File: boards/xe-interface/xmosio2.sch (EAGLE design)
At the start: 105 parts, among them IC1 IDTQS3245QSOP20, IC2 IDTQS3245QSOP20, IC3 IDTQS3245QSOP20, IC4 IDTQS3245QSOP20, IC5 IDTQS3245QSOP20, U1 24 MHz Osc. (F535L-24), U2 USD-SOCKETNEW, X1 0446200002

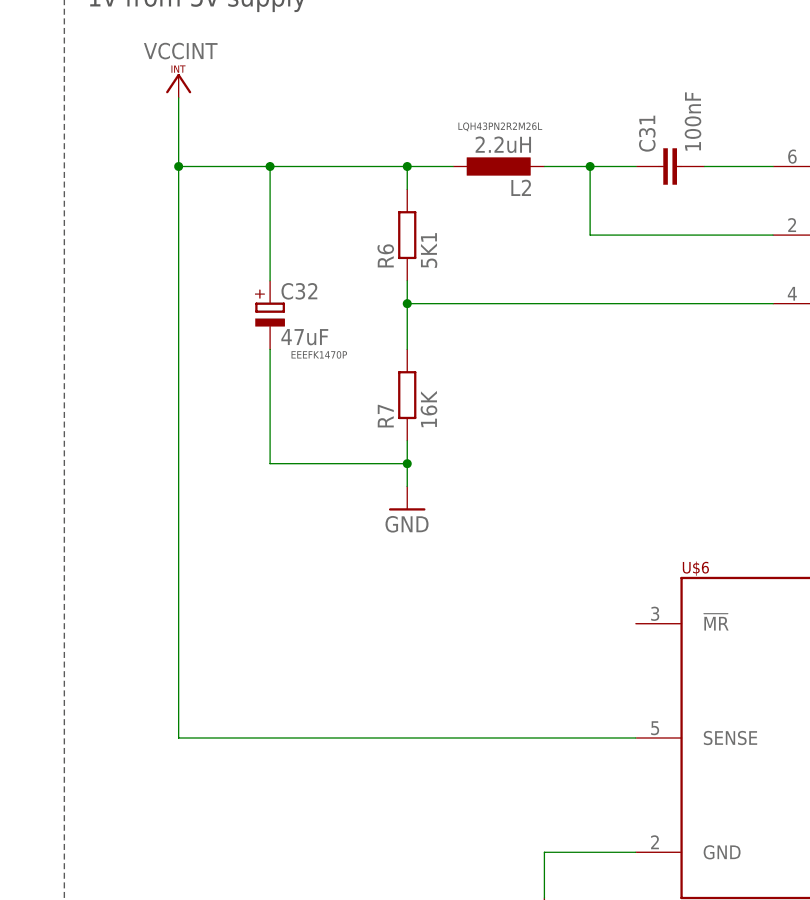
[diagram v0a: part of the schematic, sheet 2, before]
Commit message: Fix the voltage supervisor circuit, so we can bring up the 1v rail
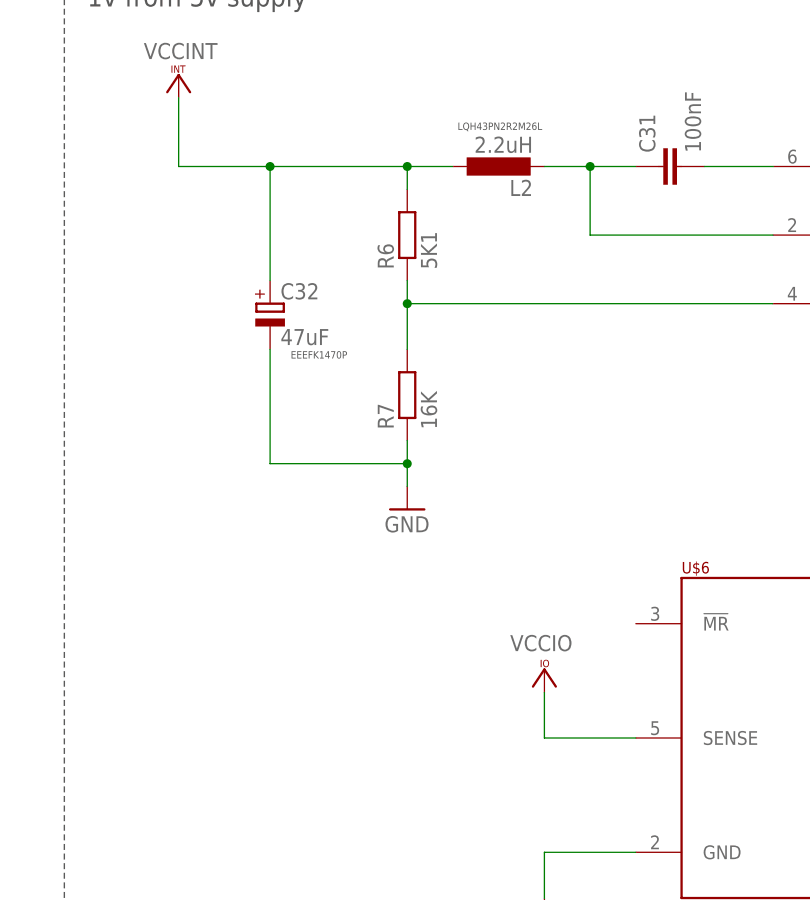
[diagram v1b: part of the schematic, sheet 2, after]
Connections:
- net VCCINT: no longer U$6.SENSE@5
- net VCCIO: now also U$6.SENSE@5
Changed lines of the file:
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@@
 <setting verticaltext="up"/>
 </settings>
-<grid distance="0.1" unitdist="inch" unit="inch" style="lines" multiple="1" display="yes" altdistance="0.01" altunitdist="inch" altunit="inch"/>
+<grid distance="0.1" unitdist="inch" unit="inch" style="lines" multiple="1" display="no" altdistance="0.01" altunitdist="inch" altunit="inch"/>
 <layers>
-<layer number="1" name="Top" color="4" fill="1" visible="yes" active="no"/>
-<layer number="2" name="Route2" color="1" fill="3" visible="yes" active="no"/>
-<layer number="3" name="Route3" color="4" fill="3" visible="yes" active="no"/>
-<layer number="14" name="Route14" color="1" fill="6" visible="yes" active="no"/>
-<layer number="15" name="Route15" color="4" fill="6" visible="yes" active="no"/>
-<layer number="16" name="Bottom" color="1" fill="1" visible="yes" active="no"/>
-<layer number="17" name="Pads" color="2" fill="1" visible="yes" active="no"/>
-<layer number="18" name="Vias" color="2" fill="1" visible="yes" active="no"/>
-<layer number="19" name="Unrouted" color="6" fill="1" visible="yes" active="no"/>
-<layer number="20" name="Dimension" color="15" fill="1" visible="yes" active="no"/>
-<layer number="21" name="tPlace" color="7" fill="1" visible="yes" active="no"/>
-<layer number="22" name="bPlace" color="7" fill="1" visible="yes" active="no"/>
-<layer number="23" name="tOrigins" color="15" fill="1" visible="yes" active="no"/>
-<layer number="24" name="bOrigins" color="15" fill="1" visible="yes" active="no"/>
-<layer number="25" name="tNames" color="7" fill="1" visible="yes" active="no"/>
-<layer number="26" name="bNames" color="7" fill="1" visible="yes" active="no"/>
-<layer number="27" name="tValues" color="7" fill="1" visible="yes" active="no"/>
-<layer number="28" name="bValues" color="7" fill="1" visible="yes" active="no"/>
+<layer number="1" name="Top" color="4" fill="1" visible="no" active="no"/>
+<layer number="2" name="Route2" color="1" fill="3" visible="no" active="no"/>
+<layer number="3" name="Route3" color="4" fill="3" visible="no" active="no"/>
+<layer number="14" name="Route14" color="1" fill="6" visible="no" active="no"/>
+<layer number="15" name="Route15" color="4" fill="6" visible="no" active="no"/>
+<layer number="16" name="Bottom" color="1" fill="1" visible="no" active="no"/>
+<layer number="17" name="Pads" color="2" fill="1" visible="no" active="no"/>
+<layer number="18" name="Vias" color="2" fill="1" visible="no" active="no"/>
+<layer number="19" name="Unrouted" color="6" fill="1" visible="no" active="no"/>
+<layer number="20" name="Dimension" color="15" fill="1" visible="no" active="no"/>
+<layer number="21" name="tPlace" color="7" fill="1" visible="no" active="no"/>
+<layer number="22" name="bPlace" color="7" fill="1" visible="no" active="no"/>
+<layer number="23" name="tOrigins" color="15" fill="1" visible="no" active="no"/>
+<layer number="24" name="bOrigins" color="15" fill="1" visible="no" active="no"/>
+<layer number="25" name="tNames" color="7" fill="1" visible="no" active="no"/>
+<layer number="26" name="bNames" color="7" fill="1" visible="no" active="no"/>
+<layer number="27" name="tValues" color="7" fill="1" visible="no" active="no"/>
+<layer number="28" name="bValues" color="7" fill="1" visible="no" active="no"/>
 <layer number="29" name="tStop" color="7" fill="3" visible="no" active="no"/>
 <layer number="30" name="bStop" color="7" fill="6" visible="no" active="no"/>
@@
 <layer number="35" name="tGlue" color="7" fill="4" visible="no" active="no"/>
 <layer number="36" name="bGlue" color="7" fill="5" visible="no" active="no"/>
-<layer number="37" name="tTest" color="7" fill="1" visible="yes" active="no"/>
-<layer number="38" name="bTest" color="7" fill="1" visible="yes" active="no"/>
+<layer number="37" name="tTest" color="7" fill="1" visible="no" active="no"/>
+<layer number="38" name="bTest" color="7" fill="1" visible="no" active="no"/>
 <layer number="39" name="tKeepout" color="4" fill="11" visible="no" active="no"/>
 <layer number="40" name="bKeepout" color="1" fill="11" visible="no" active="no"/>
@@
 <layer number="44" name="Drills" color="7" fill="1" visible="no" active="no"/>
 <layer number="45" name="Holes" color="7" fill="1" visible="no" active="no"/>
-<layer number="46" name="Milling" color="3" fill="1" visible="yes" active="no"/>
-<layer number="47" name="Measures" color="7" fill="1" visible="yes" active="no"/>
-<layer number="48" name="Document" color="7" fill="1" visible="yes" active="no"/>
-<layer number="49" name="Reference" color="7" fill="1" visible="yes" active="no"/>
-<layer number="50" name="dxf" color="7" fill="1" visible="yes" active="no"/>
-<layer number="51" name="tDocu" color="7" fill="1" visible="yes" active="no"/>
-<layer number="52" name="bDocu" color="7" fill="1" visible="yes" active="no"/>
-<layer number="53" name="tGND_GNDA" color="7" fill="9" visible="yes" active="no"/>
-<layer number="54" name="bGND_GNDA" color="1" fill="9" visible="yes" active="no"/>
-<layer number="56" name="wert" color="7" fill="1" visible="yes" active="no"/>
-<layer number="57" name="tCAD" color="7" fill="1" visible="yes" active="no"/>
+<layer number="46" name="Milling" color="3" fill="1" visible="no" active="no"/>
+<layer number="47" name="Measures" color="7" fill="1" visible="no" active="no"/>
+<layer number="48" name="Document" color="7" fill="1" visible="no" active="no"/>
+<layer number="49" name="Reference" color="7" fill="1" visible="no" active="no"/>
+<layer number="50" name="dxf" color="7" fill="1" visible="no" active="no"/>
+<layer number="51" name="tDocu" color="7" fill="1" visible="no" active="no"/>
+<layer number="52" name="bDocu" color="7" fill="1" visible="no" active="no"/>
+<layer number="53" name="tGND_GNDA" color="7" fill="9" visible="no" active="no"/>
+<layer number="54" name="bGND_GNDA" color="1" fill="9" visible="no" active="no"/>
+<layer number="56" name="wert" color="7" fill="1" visible="no" active="no"/>
+<layer number="57" name="tCAD" color="7" fill="1" visible="no" active="no"/>
 <layer number="90" name="Modules" color="5" fill="1" visible="yes" active="yes"/>
 <layer number="91" name="Nets" color="2" fill="1" visible="yes" active="yes"/>
@@
 <part name="R16" library="rcl" deviceset="R-EU_" device="R0603" value="0R"/>
 <part name="R17" library="rcl" deviceset="R-EU_" device="R0603" value="0R"/>
+<part name="VCC26" library="supply1" deviceset="VCCIO" device=""/>
 </parts>
 <sheets>
@@
 <attribute name="VALUE" x="298.45" y="-36.068" size="1.778" layer="96"/>
 </instance>
+<instance part="VCC26" gate="G$1" x="208.28" y="-60.96" smashed="yes">
+<attribute name="VALUE" x="204.47" y="-58.928" size="1.778" layer="96"/>
+</instance>
 </instances>
 <busses>
@@
 <wire x1="167.64" y1="-5.08" x2="177.8" y2="-5.08" width="0.1524" layer="91"/>
 <junction x="177.8" y="-5.08"/>
-<wire x1="167.64" y1="-68.58" x2="167.64" y2="-5.08" width="0.1524" layer="91"/>
-<pinref part="U$6" gate="G$1" pin="SENSE@5"/>
-<wire x1="167.64" y1="-68.58" x2="218.44" y2="-68.58" width="0.1524" layer="91"/>
 <pinref part="VCC10" gate="G$1" pin="VCCINT"/>
 <wire x1="167.64" y1="2.54" x2="167.64" y2="-5.08" width="0.1524" layer="91"/>
-<junction x="167.64" y="-5.08"/>
 </segment>
 </net>
@@
 <pinref part="VCC24" gate="G$1" pin="VCCIO"/>
 </segment>
-</net>
+<segment>
+<pinref part="U$6" gate="G$1" pin="SENSE@5"/>
+<pinref part="VCC26" gate="G$1" pin="VCCIO"/>
+<wire x1="218.44" y1="-68.58" x2="208.28" y2="-68.58" width="0.1524" layer="91"/>
+<wire x1="208.28" y1="-68.58" x2="208.28" y2="-63.5" width="0.1524" layer="91"/>
+</segment>
+</net>

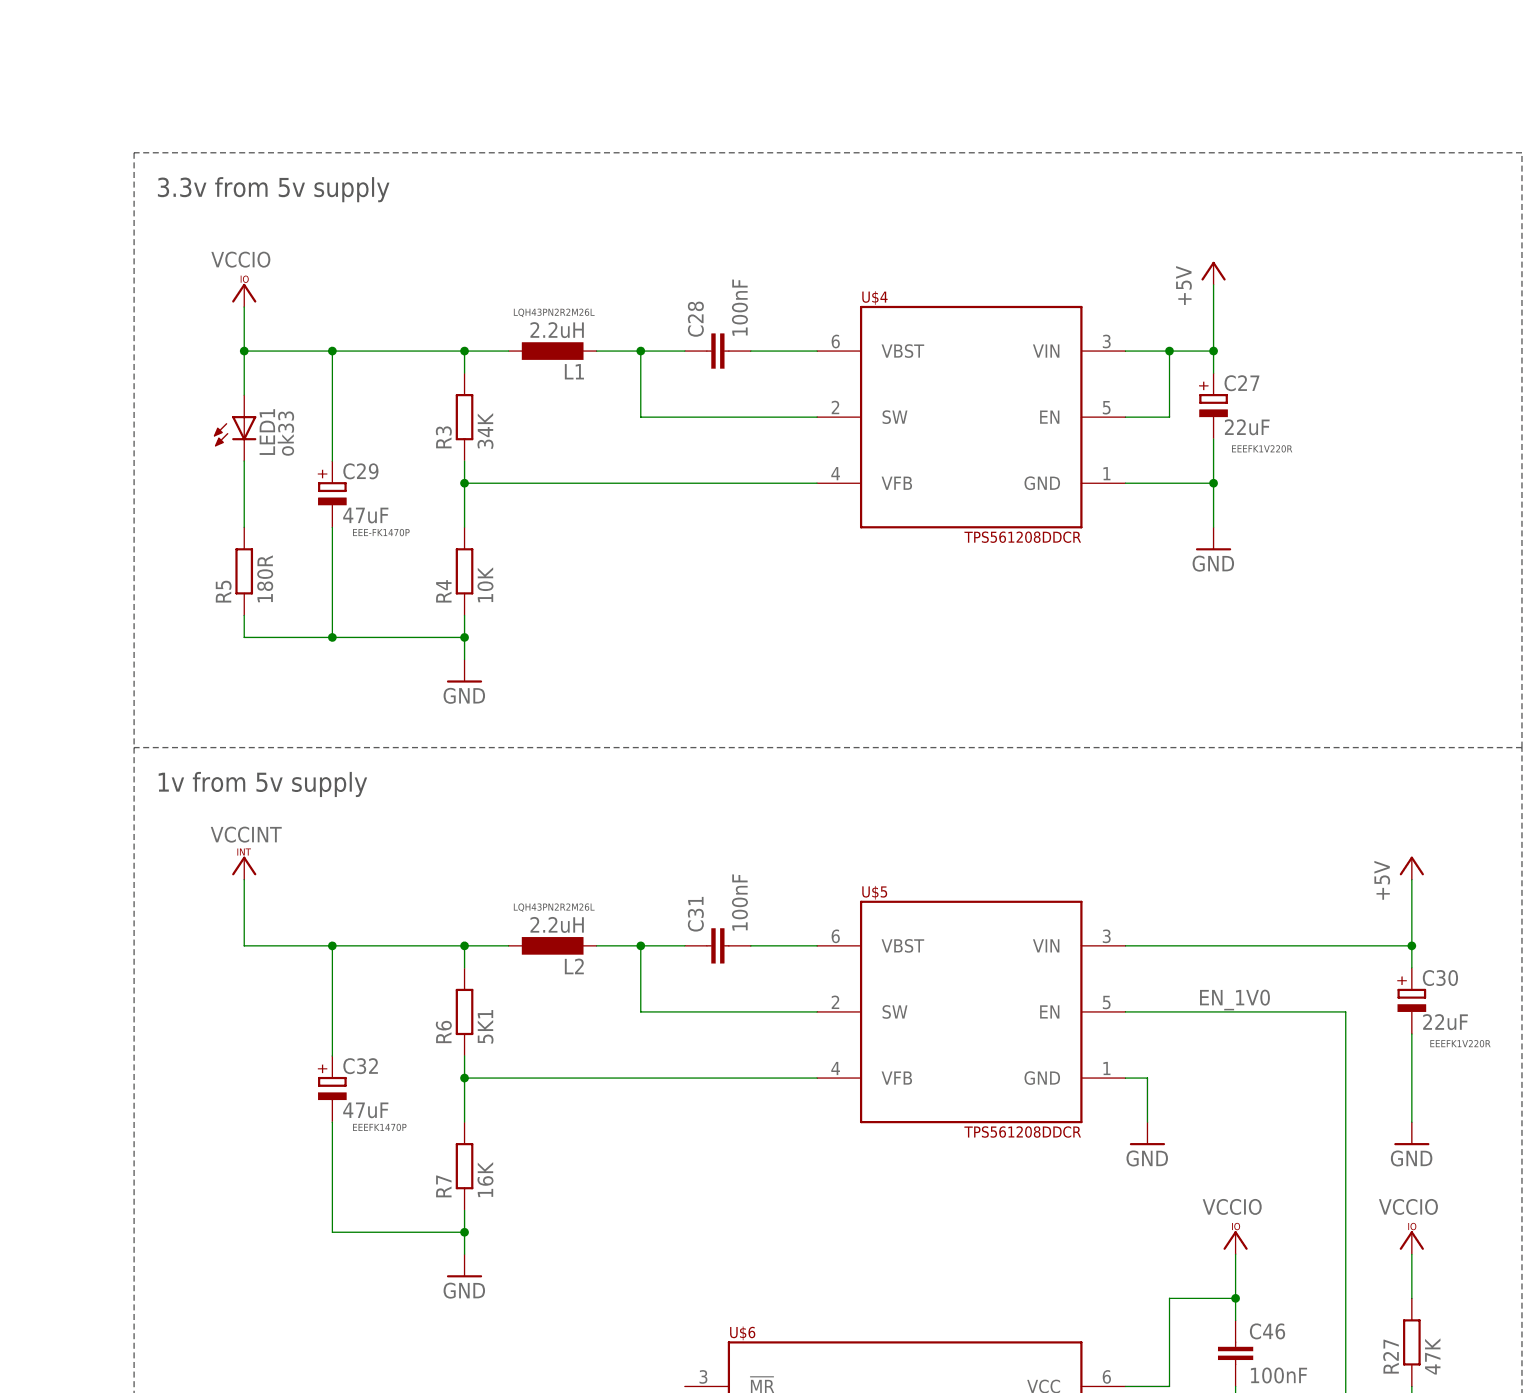
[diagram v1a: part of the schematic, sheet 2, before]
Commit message: Move to a SeeedStudio style layout (far cheaper, and we can get assembly as part of the package). We still require the 5/5 spacing though.
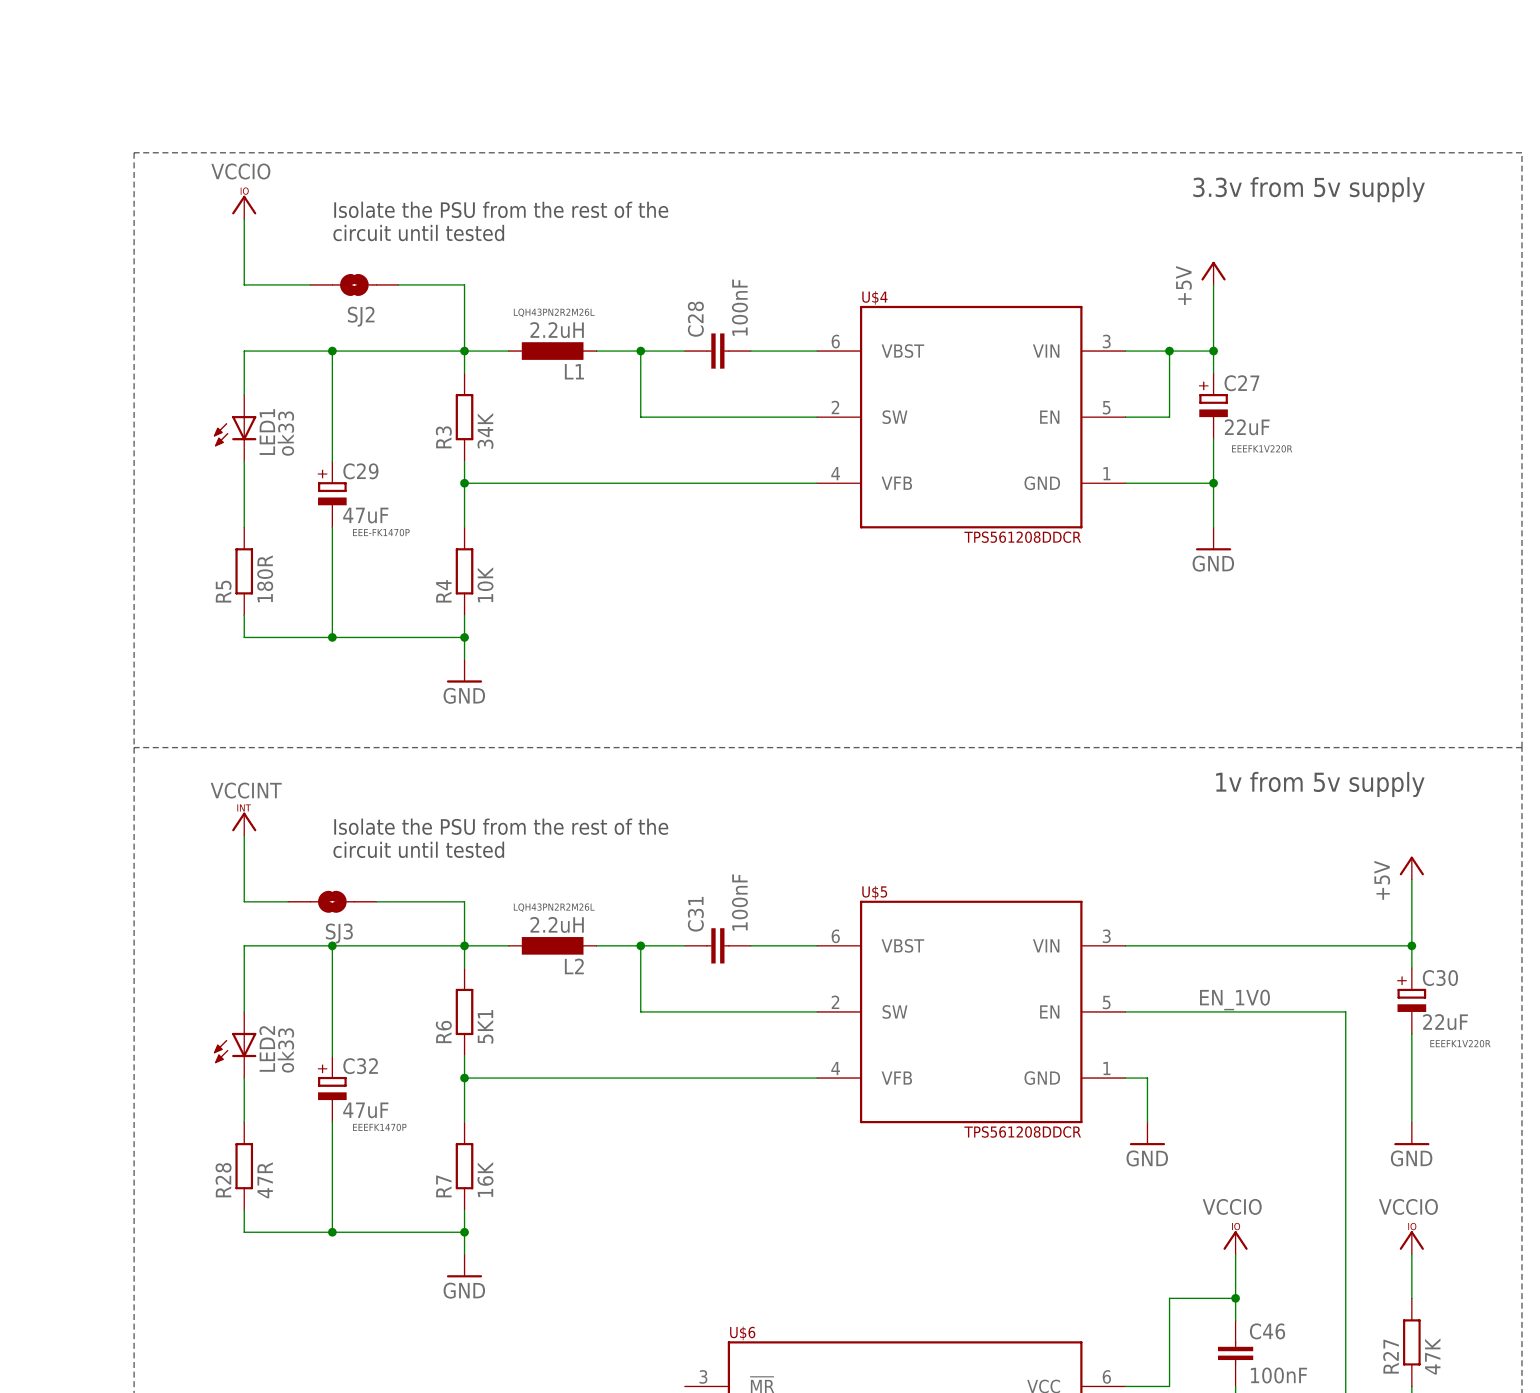
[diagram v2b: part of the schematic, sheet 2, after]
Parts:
- added LED2: ok33, led:LEDCHIP-LED0805
- added R28: 47R, rcl:R-EU_R1206
- added SJ2, SJ3: SOLDERJUMPERNO, SparkFun:SOLDERJUMPERNO
- C1, C10, C11, C12, C13, C14, C15, C16, C17, C18, C19, C2, C20, C21, C22, C23, C24, C25, C26, C28, C3, C31, C34, C35, C36, C37, C38, C39, C4, C40, C41, C42, C43, C44, C45, C46, C5, C6, C7, C8, C9: device rcl:C-EUC0603 -> rcl:C-EUC1206
- R1, R10, R11, R12, R13, R14, R15, R16, R17, R18, R19, R2, R20, R21, R22, R23, R24, R25, R26, R27, R3, R4, R5, R6, R7, R8, R9: device rcl:R-EU_R0603 -> rcl:R-EU_R1206
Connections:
- new net N$30: C29.+, L1.1, LED1.A, R3.2, SJ2.1
- new net N$31: LED2.C, R28.2
- new net N$32: C32.+, L2.1, LED2.A, R6.2, SJ3.1
- net GND: now also R28.1
- net VCCINT: now also SJ3.2; no longer C32.+, L2.1, R6.2
- net VCCIO: now also SJ2.2; no longer C29.+, L1.1, LED1.A, R3.2
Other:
- note added: "Isolate the PSU from the rest of the circuit until tested"
